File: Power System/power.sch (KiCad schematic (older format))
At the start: 35 parts, among them J1 PC104_40Pin_2.54mm, J2 Charge Cable, J3 Battery Pack, J4 IDC Header, U1 ds2781e+, U2 LT3461AES6-TRPBF

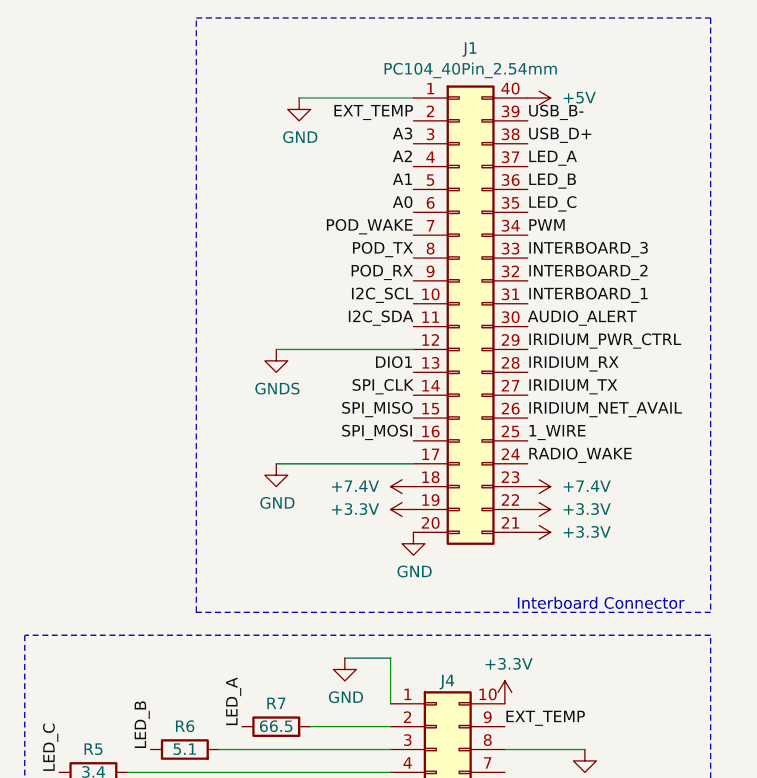
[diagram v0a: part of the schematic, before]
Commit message: Renamed pins on through-board connector
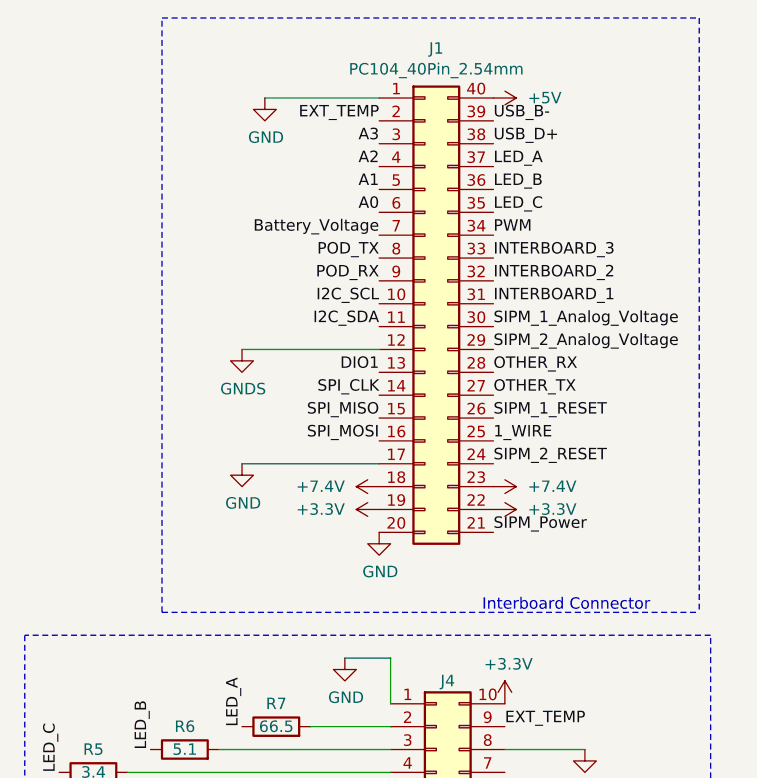
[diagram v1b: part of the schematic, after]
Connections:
- net +3V3: no longer J1.21 (Pin_21)
- net SIPM_Power: now also J1.21 (Pin_21)
- net AUDIO_ALERT renamed SIPM_1_Analog_Voltage
- net IRIDIUM_NET_AVAIL renamed SIPM_1_RESET
- net IRIDIUM_PWR_CTRL renamed SIPM_2_Analog_Voltage
- net IRIDIUM_RX renamed OTHER_RX
- net IRIDIUM_TX renamed OTHER_TX
- net POD_WAKE renamed Battery_Voltage
- net RADIO_WAKE renamed SIPM_2_RESET
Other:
- moved on the sheet: J1
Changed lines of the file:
@@
 Wire Wire Line
 	3000 7650 3000 7750
-Text Label 9650 2200 0    50   ~ 0
-IRIDIUM_TX
-Text Label 9650 2100 0    50   ~ 0
-IRIDIUM_RX
-Text Label 9650 2400 0    50   ~ 0
-1_WIRE
-Text Label 9650 2000 0    50   ~ 0
-IRIDIUM_PWR_CTRL
-Text Label 9650 2300 0    50   ~ 0
-IRIDIUM_NET_AVAIL
-Text Label 9150 2400 2    50   ~ 0
-SPI_MOSI
-Text Label 9150 2300 2    50   ~ 0
-SPI_MISO
-Text Label 9150 2200 2    50   ~ 0
-SPI_CLK
-Text Label 9150 1900 2    50   ~ 0
-I2C_SDA
-Text Label 9150 1800 2    50   ~ 0
-I2C_SCL
-Text Label 9650 1200 0    50   ~ 0
-LED_A
-Text Label 9650 1300 0    50   ~ 0
-LED_B
-Text Label 9650 1400 0    50   ~ 0
-LED_C
-Text Label 9150 1400 2    50   ~ 0
-A0
-Text Label 9150 1300 2    50   ~ 0
-A1
-Text Label 9150 1200 2    50   ~ 0
-A2
-Text Label 9650 1500 0    50   ~ 0
-PWM
-Text Label 9150 2100 2    50   ~ 0
-DIO1
-Text Label 9650 2500 0    50   ~ 0
-RADIO_WAKE
-Text Label 9650 1100 0    50   ~ 0
-USB_D+
-Text Label 9650 1000 0    50   ~ 0
-USB_B-
-Text Label 9150 1500 2    50   ~ 0
-POD_WAKE
-Text Label 9150 1700 2    50   ~ 0
-POD_RX
-Text Label 9150 1600 2    50   ~ 0
-POD_TX
-$Comp
-L power:+5V #PWR0106
-U 1 1 5DBA9AD1
-P 9650 900
-F 0 "#PWR0106" H 9650 750 50  0001 C CNN
-F 1 "+5V" V 9650 1050 50  0000 L CNN
-F 2 "" H 9650 900 50  0001 C CNN
-F 3 "" H 9650 900 50  0001 C CNN
-	1    9650 900
-	0    1    1    0
-$EndComp
-$Comp
-L power:GND #PWR0107
-U 1 1 5DBAA285
-P 8650 900
-F 0 "#PWR0107" H 8650 650 50  0001 C CNN
-F 1 "GND" H 8655 727 50  0000 C CNN
-F 2 "" H 8650 900 50  0001 C CNN
-F 3 "" H 8650 900 50  0001 C CNN
-	1    8650 900
-	1    0    0    -1
-$EndComp
-$Comp
-L power:GNDS #PWR0108
-U 1 1 5DBABCBA
-P 8550 2000
-F 0 "#PWR0108" H 8550 1750 50  0001 C CNN
-F 1 "GNDS" H 8555 1827 50  0000 C CNN
-F 2 "" H 8550 2000 50  0001 C CNN
-F 3 "" H 8550 2000 50  0001 C CNN
-	1    8550 2000
-	1    0    0    -1
-$EndComp
-$Comp
-L power:GND #PWR0110
-U 1 1 5DBB128C
-P 9150 2800
-F 0 "#PWR0110" H 9150 2550 50  0001 C CNN
-F 1 "GND" H 9155 2627 50  0000 C CNN
-F 2 "" H 9150 2800 50  0001 C CNN
-F 3 "" H 9150 2800 50  0001 C CNN
-	1    9150 2800
-	1    0    0    -1
-$EndComp
-$Comp
-L power-rescue:PC104_40Pin_2.54mm-WhitworthStandard-power-rescue-power-rescue-power-rescue-power-rescue-power-rescue-power-rescue J1
-U 1 1 5DB909C2
-P 9350 1800
-F 0 "J1" H 9400 2917 50  0000 C CNN
-F 1 "PC104_40Pin_2.54mm" H 9400 2826 50  0000 C CNN
-F 2 "WhitworthStandard:PC104_40PinSocket_2.54mm" H 9350 1800 50  0001 C CNN
-F 3 "~" H 9350 1800 50  0001 C CNN
-	1    9350 1800
-	1    0    0    -1
-$EndComp
-Text Label 9150 1000 2    50   ~ 0
-EXT_TEMP
-Text Label 9150 1100 2    50   ~ 0
-A3
 $Comp
 L power:GNDPWR #PWR0116
@@
 Wire Wire Line
 	4000 7650 4000 7800
-Wire Notes Line
-	8200 550  10450 550
-Wire Notes Line
-	10450 550  10450 3150
-Text Notes 9600 3150 0    50   ~ 0
-Interboard Connector
-Wire Wire Line
-	9150 2000 8550 2000
-Text Label 9650 1800 0    50   ~ 0
-INTERBOARD_1
-Text Label 9650 1700 0    50   ~ 0
-INTERBOARD_2
-Text Label 9650 1900 0    50   ~ 0
-AUDIO_ALERT
-Text Label 9650 1600 0    50   ~ 0
-INTERBOARD_3
-Wire Notes Line
-	8200 3150 8200 550
-Wire Notes Line
-	10450 3150 8200 3150
 $Comp
 L Connector_Generic:Conn_02x05_Counter_Clockwise J4
@@
 	1    0    0    -1
 $EndComp
-Wire Wire Line
-	8650 900  9150 900
 Text Label 9550 3650 0    50   ~ 0
 EXT_TEMP
@@
 Wire Wire Line
 	1800 1600 2050 1600
-$Comp
-L power:+3.3V #PWR0109
-U 1 1 5E718EAD
-P 9650 2800
-F 0 "#PWR0109" H 9650 2650 50  0001 C CNN
-F 1 "+3.3V" V 9650 2950 50  0000 L CNN
-F 2 "" H 9650 2800 50  0001 C CNN
-F 3 "" H 9650 2800 50  0001 C CNN
-	1    9650 2800
-	0    1    1    0
-$EndComp
-Wire Wire Line
-	8550 2500 9150 2500
-$Comp
-L WhitworthStandard:+7.4V #PWR0114
-U 1 1 5E1EC1FF
-P 9650 2600
-F 0 "#PWR0114" H 9650 2450 50  0001 C CNN
-F 1 "+7.4V" V 9650 2750 50  0000 L CNN
-F 2 "" H 9650 2600 50  0001 C CNN
-F 3 "" H 9650 2600 50  0001 C CNN
-	1    9650 2600
-	0    1    1    0
-$EndComp
-$Comp
-L WhitworthStandard:+7.4V #PWR0112
-U 1 1 5E1E31F7
-P 9150 2600
-F 0 "#PWR0112" H 9150 2450 50  0001 C CNN
-F 1 "+7.4V" V 9150 2750 50  0000 L CNN
-F 2 "" H 9150 2600 50  0001 C CNN
-F 3 "" H 9150 2600 50  0001 C CNN
-	1    9150 2600
-	0    -1   -1   0
-$EndComp
-$Comp
-L power:+3.3V #PWR0123
-U 1 1 5E90BE99
-P 9650 2700
-F 0 "#PWR0123" H 9650 2550 50  0001 C CNN
-F 1 "+3.3V" V 9650 2850 50  0000 L CNN
-F 2 "" H 9650 2700 50  0001 C CNN
-F 3 "" H 9650 2700 50  0001 C CNN
-	1    9650 2700
-	0    1    1    0
-$EndComp
-$Comp
-L power:+3.3V #PWR0137
-U 1 1 5E90C21A
-P 9150 2700
-F 0 "#PWR0137" H 9150 2550 50  0001 C CNN
-F 1 "+3.3V" V 9150 2850 50  0000 L CNN
-F 2 "" H 9150 2700 50  0001 C CNN
-F 3 "" H 9150 2700 50  0001 C CNN
-	1    9150 2700
-	0    -1   1    0
-$EndComp
-$Comp
-L power:GND #PWR0139
-U 1 1 5E90F9C2
-P 8550 2500
-F 0 "#PWR0139" H 8550 2250 50  0001 C CNN
-F 1 "GND" H 8555 2327 50  0000 C CNN
-F 2 "" H 8550 2500 50  0001 C CNN
-F 3 "" H 8550 2500 50  0001 C CNN
-	1    8550 2500
-	1    0    0    -1
-$EndComp
 Wire Notes Line
 	550  550  6000 550
@@
 Text Notes 5450 7400 0    50   ~ 0
 DC-DC Booster
+Text Label 9500 2800 0    50   ~ 0
+SIPM_Power
+$Comp
+L power:GND #PWR0139
+U 1 1 5E90F9C2
+P 8400 2500
+F 0 "#PWR0139" H 8400 2250 50  0001 C CNN
+F 1 "GND" H 8405 2327 50  0000 C CNN
+F 2 "" H 8400 2500 50  0001 C CNN
+F 3 "" H 8400 2500 50  0001 C CNN
+	1    8400 2500
+	1    0    0    -1
+$EndComp
+$Comp
+L power:+3.3V #PWR0137
+U 1 1 5E90C21A
+P 9000 2700
+F 0 "#PWR0137" H 9000 2550 50  0001 C CNN
+F 1 "+3.3V" V 9000 2850 50  0000 L CNN
+F 2 "" H 9000 2700 50  0001 C CNN
+F 3 "" H 9000 2700 50  0001 C CNN
+	1    9000 2700
+	0    -1   1    0
+$EndComp
+$Comp
+L power:+3.3V #PWR0123
+U 1 1 5E90BE99
+P 9500 2700
+F 0 "#PWR0123" H 9500 2550 50  0001 C CNN
+F 1 "+3.3V" V 9500 2850 50  0000 L CNN
+F 2 "" H 9500 2700 50  0001 C CNN
+F 3 "" H 9500 2700 50  0001 C CNN
+	1    9500 2700
+	0    1    1    0
+$EndComp
+$Comp
+L WhitworthStandard:+7.4V #PWR0112
+U 1 1 5E1E31F7
+P 9000 2600
+F 0 "#PWR0112" H 9000 2450 50  0001 C CNN
+F 1 "+7.4V" V 9000 2750 50  0000 L CNN
+F 2 "" H 9000 2600 50  0001 C CNN
+F 3 "" H 9000 2600 50  0001 C CNN
+	1    9000 2600
+	0    -1   -1   0
+$EndComp
+$Comp
+L WhitworthStandard:+7.4V #PWR0114
+U 1 1 5E1EC1FF
+P 9500 2600
+F 0 "#PWR0114" H 9500 2450 50  0001 C CNN
+F 1 "+7.4V" V 9500 2750 50  0000 L CNN
+F 2 "" H 9500 2600 50  0001 C CNN
+F 3 "" H 9500 2600 50  0001 C CNN
+	1    9500 2600
+	0    1    1    0
+$EndComp
+Wire Wire Line
+	8400 2500 9000 2500
+Wire Wire Line
+	8500 900  9000 900
+Wire Notes Line
+	8050 3150 8050 550
+Text Label 9500 1600 0    50   ~ 0
+INTERBOARD_3
+Text Label 9500 1900 0    50   ~ 0
+SIPM_1_Analog_Voltage
+Text Label 9500 1700 0    50   ~ 0
+INTERBOARD_2
+Text Label 9500 1800 0    50   ~ 0
+INTERBOARD_1
+Wire Wire Line
+	9000 2000 8400 2000
+Text Notes 9450 3150 0    50   ~ 0
+Interboard Connector
+Wire Notes Line
+	10400 550  10400 3150
+Text Label 9000 1100 2    50   ~ 0
+A3
+Text Label 9000 1000 2    50   ~ 0
+EXT_TEMP
+$Comp
+L power-rescue:PC104_40Pin_2.54mm-WhitworthStandard-power-rescue-power-rescue-power-rescue-power-rescue-power-rescue-power-rescue J1
+U 1 1 5DB909C2
+P 9200 1800
+F 0 "J1" H 9250 2917 50  0000 C CNN
+F 1 "PC104_40Pin_2.54mm" H 9250 2826 50  0000 C CNN
+F 2 "WhitworthStandard:PC104_40PinSocket_2.54mm" H 9200 1800 50  0001 C CNN
+F 3 "~" H 9200 1800 50  0001 C CNN
+	1    9200 1800
+	1    0    0    -1
+$EndComp
+$Comp
+L power:GND #PWR0110
+U 1 1 5DBB128C
+P 9000 2800
+F 0 "#PWR0110" H 9000 2550 50  0001 C CNN
+F 1 "GND" H 9005 2627 50  0000 C CNN
+F 2 "" H 9000 2800 50  0001 C CNN
+F 3 "" H 9000 2800 50  0001 C CNN
+	1    9000 2800
+	1    0    0    -1
+$EndComp
+$Comp
+L power:GNDS #PWR0108
+U 1 1 5DBABCBA
+P 8400 2000
+F 0 "#PWR0108" H 8400 1750 50  0001 C CNN
+F 1 "GNDS" H 8405 1827 50  0000 C CNN
+F 2 "" H 8400 2000 50  0001 C CNN
+F 3 "" H 8400 2000 50  0001 C CNN
+	1    8400 2000
+	1    0    0    -1
+$EndComp
+$Comp
+L power:GND #PWR0107
+U 1 1 5DBAA285
+P 8500 900
+F 0 "#PWR0107" H 8500 650 50  0001 C CNN
+F 1 "GND" H 8505 727 50  0000 C CNN
+F 2 "" H 8500 900 50  0001 C CNN
+F 3 "" H 8500 900 50  0001 C CNN
+	1    8500 900
+	1    0    0    -1
+$EndComp
+$Comp
+L power:+5V #PWR0106
+U 1 1 5DBA9AD1
+P 9500 900
+F 0 "#PWR0106" H 9500 750 50  0001 C CNN
+F 1 "+5V" V 9500 1050 50  0000 L CNN
+F 2 "" H 9500 900 50  0001 C CNN
+F 3 "" H 9500 900 50  0001 C CNN
+	1    9500 900
+	0    1    1    0
+$EndComp
+Text Label 9000 1600 2    50   ~ 0
+POD_TX
+Text Label 9000 1700 2    50   ~ 0
+POD_RX
+Text Label 9000 1500 2    50   ~ 0
+Battery_Voltage
+Text Label 9500 1000 0    50   ~ 0
+USB_B-
+Text Label 9500 1100 0    50   ~ 0
+USB_D+
+Text Label 9500 2500 0    50   ~ 0
+SIPM_2_RESET
+Text Label 9000 2100 2    50   ~ 0
+DIO1
+Text Label 9500 1500 0    50   ~ 0
+PWM
+Text Label 9000 1200 2    50   ~ 0
+A2
+Text Label 9000 1300 2    50   ~ 0
+A1
+Text Label 9000 1400 2    50   ~ 0
+A0
+Text Label 9500 1400 0    50   ~ 0
+LED_C
+Text Label 9500 1300 0    50   ~ 0
+LED_B
+Text Label 9500 1200 0    50   ~ 0
+LED_A
+Text Label 9000 1800 2    50   ~ 0
+I2C_SCL
+Text Label 9000 1900 2    50   ~ 0
+I2C_SDA
+Text Label 9000 2200 2    50   ~ 0
+SPI_CLK
+Text Label 9000 2300 2    50   ~ 0
+SPI_MISO
+Text Label 9000 2400 2    50   ~ 0
+SPI_MOSI
+Text Label 9500 2300 0    50   ~ 0
+SIPM_1_RESET
+Text Label 9500 2000 0    50   ~ 0
+SIPM_2_Analog_Voltage
+Text Label 9500 2400 0    50   ~ 0
+1_WIRE
+Text Label 9500 2100 0    50   ~ 0
+OTHER_RX
+Text Label 9500 2200 0    50   ~ 0
+OTHER_TX
+Wire Notes Line
+	8050 550  10400 550
+Wire Notes Line
+	8050 3150 10400 3150
 $EndSCHEMATC

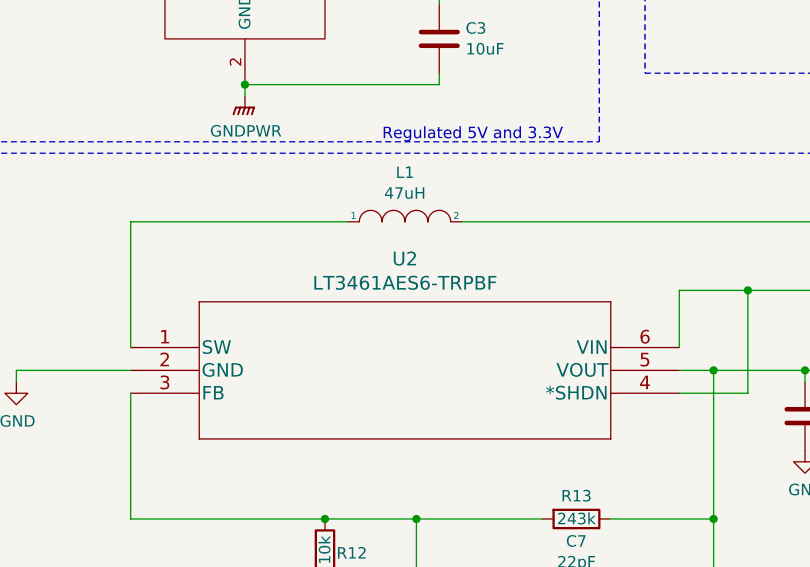
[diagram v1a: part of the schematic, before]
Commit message: Swapped LT3461a for LT3461 and changed pins on connector
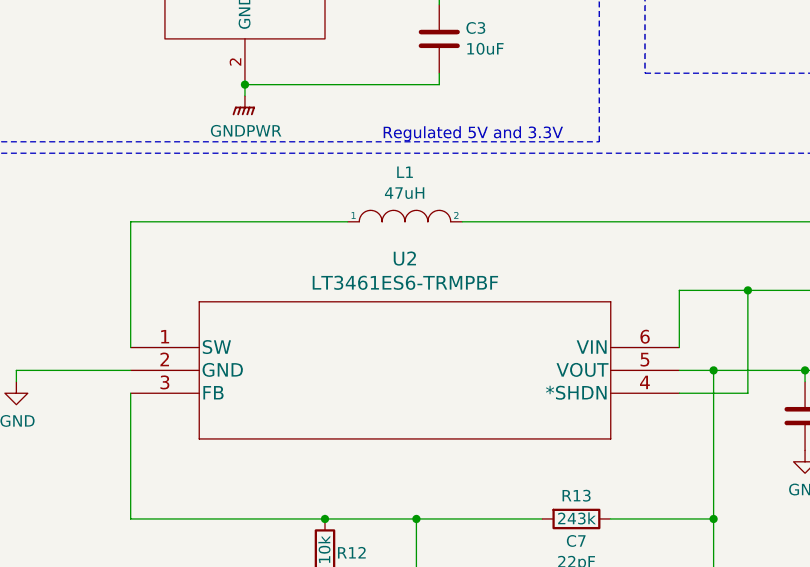
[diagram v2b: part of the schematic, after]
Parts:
- removed U2: LT3461AES6-TRPBF, LT3461AES6-TRPBF:LT3461AES6-TRPBF, symbol LT3461AES6-TRPBF?:LT3461AES6-TRPBF
- added U2: LT3461ES6-TRMPBF, LT3461ES6_TRMPBF:LT3461ES6-TRMPBF, symbol LT3461ES6-TRPBF:LT3461ES6-TRMPBF
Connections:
- net +5V: now also U2.4 (*SHDN), U2.6 (VIN)
- net GND: now also U2.2 (GND)
- net at L1.1: now also U2.1 (SW)
- net at C7.2, R12.1, R13.2: now also U2.3 (FB)
- net at C7.1, C8.1, FB1.2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: now also U2.5 (VOUT)
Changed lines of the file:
@@
-	1    0    0    -1
-$EndComp
-$Comp
-L LT3461AES6-TRPBF?:LT3461AES6-TRPBF U2
-U 1 1 61956E7D
-P 1150 6050
-F 0 "U2" H 2350 6437 60  0000 C CNN
-F 1 "LT3461AES6-TRPBF" H 2350 6331 60  0000 C CNN
-F 2 "LT3461AES6-TRPBF:LT3461AES6-TRPBF" H 2350 6290 60  0001 C CNN
-F 3 "" H 1150 6050 60  0000 C CNN
-	1    1150 6050
 	1    0    0    -1
 $EndComp
@@
 Wire Notes Line
 	8050 3150 10400 3150
+$Comp
+L LT3461ES6-TRPBF:LT3461ES6-TRMPBF U2
+U 1 1 61BA5F33
+P 1150 6050
+F 0 "U2" H 2350 6437 60  0000 C CNN
+F 1 "LT3461ES6-TRMPBF" H 2350 6331 60  0000 C CNN
+F 2 "LT3461ES6_TRMPBF:LT3461ES6-TRMPBF" H 2350 6290 60  0001 C CNN
+F 3 "" H 1150 6050 60  0000 C CNN
+	1    1150 6050
+	1    0    0    -1
+$EndComp
 $EndSCHEMATC

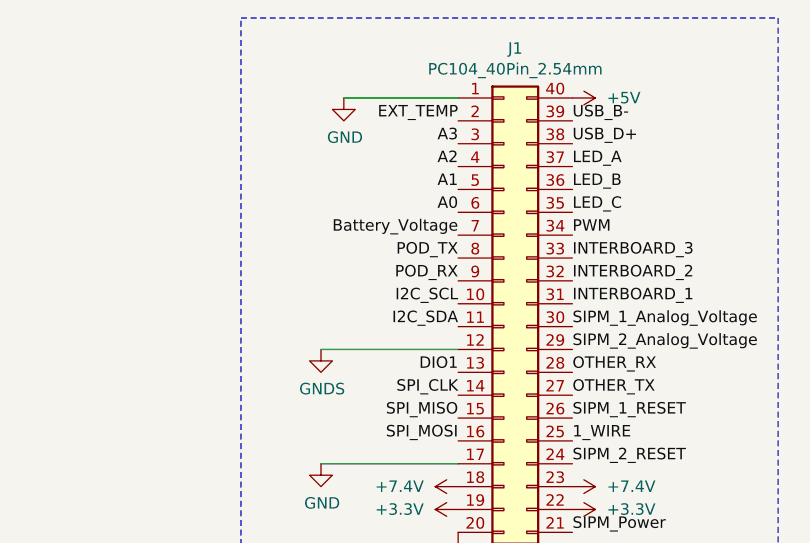
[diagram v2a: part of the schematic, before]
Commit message: Changed POD_TX and POD_RX to SERIAL_RX and SERIAL_TX
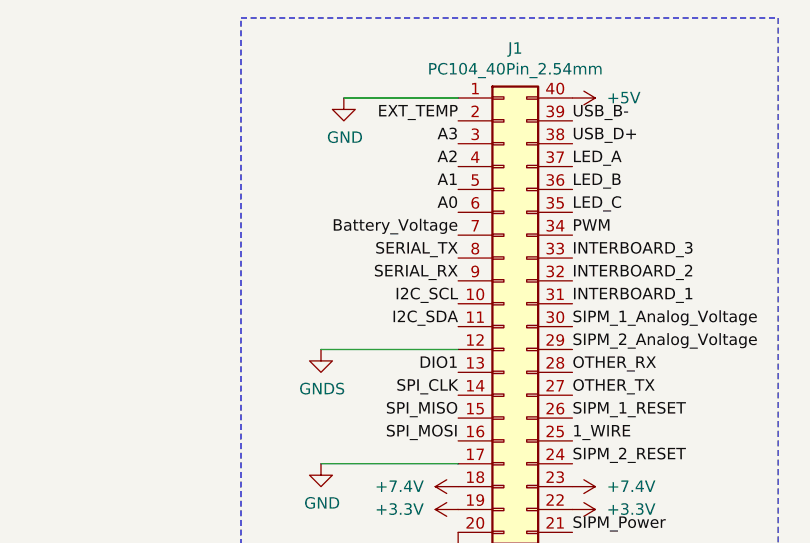
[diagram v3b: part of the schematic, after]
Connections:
- net POD_RX renamed SERIAL_RX
- net POD_TX renamed SERIAL_TX
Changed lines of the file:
@@
 $EndComp
 Text Label 9000 1600 2    50   ~ 0
-POD_TX
+SERIAL_TX
 Text Label 9000 1700 2    50   ~ 0
-POD_RX
+SERIAL_RX
 Text Label 9000 1500 2    50   ~ 0
 Battery_Voltage

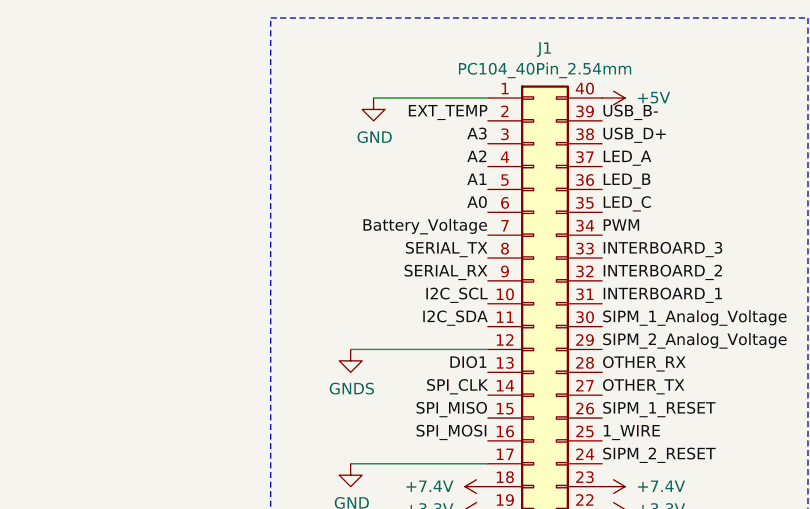
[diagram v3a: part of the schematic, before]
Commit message: Routed SIPM_Power and renamed Battery Voltage to unclaimed
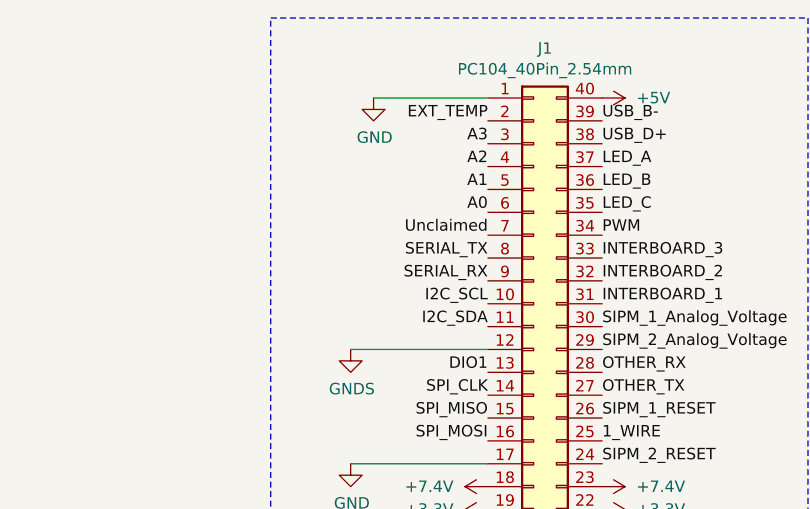
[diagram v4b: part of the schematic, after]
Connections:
- net Battery_Voltage renamed Unclaimed
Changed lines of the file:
@@
 SERIAL_RX
 Text Label 9000 1500 2    50   ~ 0
-Battery_Voltage
+Unclaimed
 Text Label 9500 1000 0    50   ~ 0
 USB_B-
